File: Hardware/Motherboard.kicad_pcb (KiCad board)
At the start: 2 copper layers, 132.1 x 81.3 mm, 51 parts, among them J1 BME680, J2 Conn_01x05_Male, J3 Display_1, J4 Display_2, J5 Buttons, J6 USB, Q1 DMG3414U, SW1 Button_Plus, SW2 Button_Minus, SW3 Button_Settings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

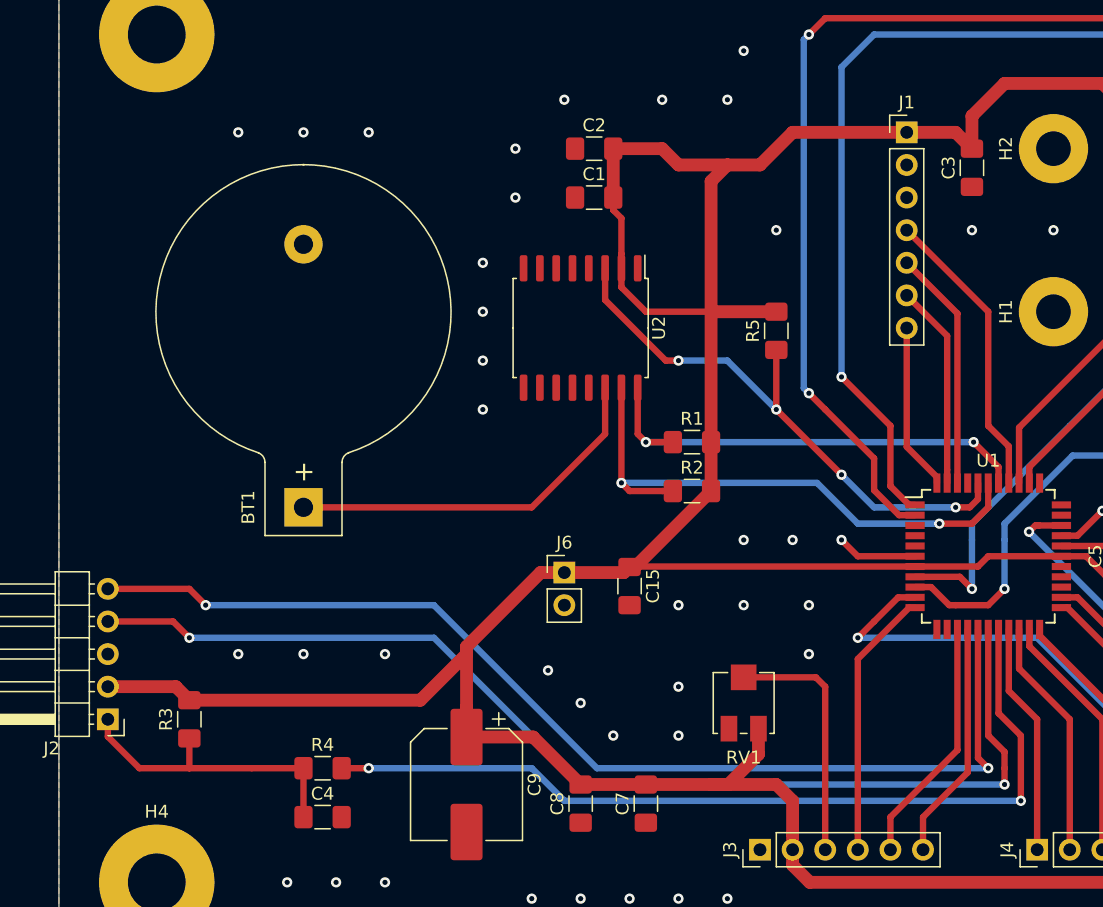
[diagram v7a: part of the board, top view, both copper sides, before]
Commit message: [Hardware] Swapped programming connector to have it in the right order.
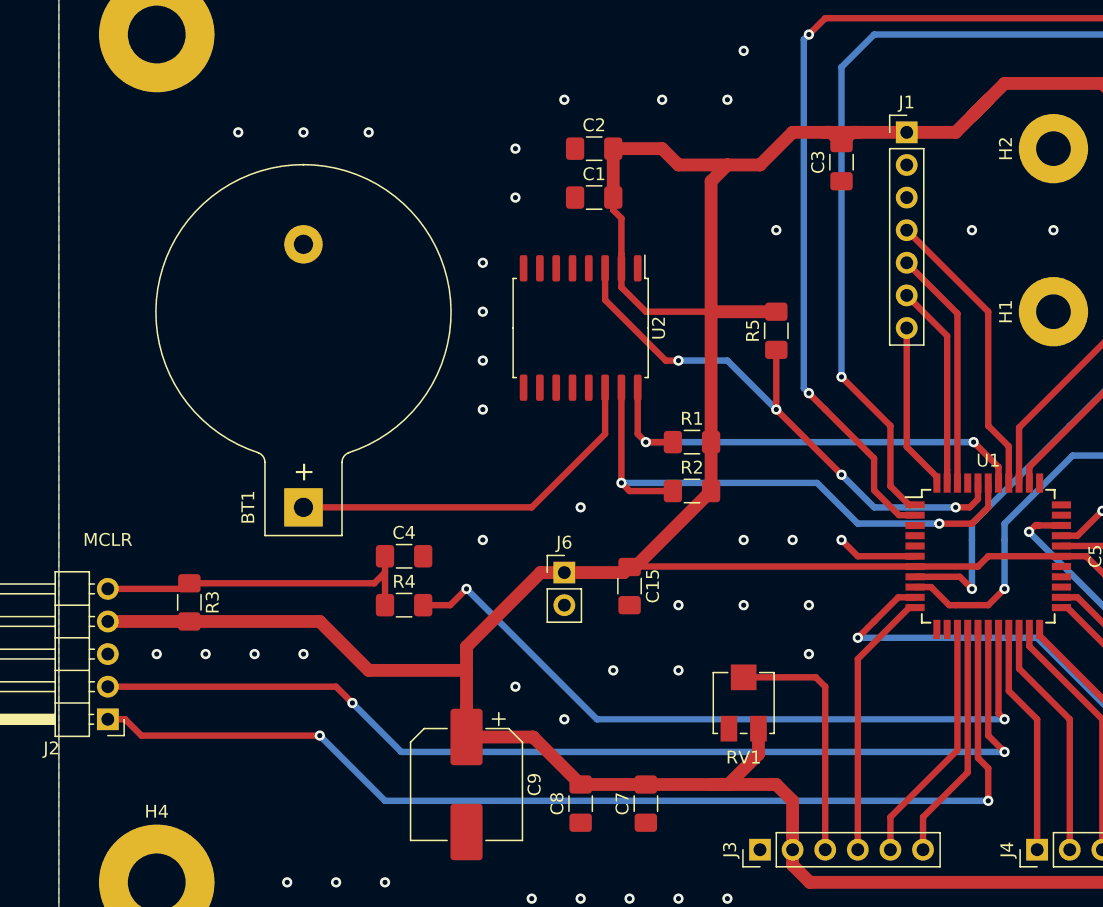
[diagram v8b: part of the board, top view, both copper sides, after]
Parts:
- J2: value Conn_01x05_Male -> JTAG
- moved C4 21.3 mm to (147.5, 55.9)
- moved R4 14.2 mm to (147.5, 59.7)
- moved C3 10.2 mm to (181.6, 25.2)
- moved R3 9.11 mm to (130.8, 59.5), turned to 270 degrees
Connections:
- H3 pad 1: Net-(H3-Pad1) -> GND
- H4 pad 1: Net-(H4-Pad1) -> GND
- H5 pad 1: Net-(H5-Pad1) -> GND
- H6 pad 1: Net-(H6-Pad1) -> GND
- J2 pad 1: Net-(C4-Pad1) -> Net-(J2-Pad1)
- J2 pad 2: +5V -> Net-(J2-Pad2)
- J2 pad 4: Net-(J2-Pad4) -> +5V
- J2 pad 5: Net-(J2-Pad5) -> Net-(C4-Pad1)
- U1 pad 16: Net-(J2-Pad5) -> Net-(J2-Pad1)
- U1 pad 17: Net-(J2-Pad4) -> Net-(J2-Pad2)
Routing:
- net Net-(J2-Pad4): track 87.7 -> 0.00 mm, vias 2 -> 0
- net Net-(J2-Pad5): track 85.5 -> 0.00 mm, vias 2 -> 0
- net Net-(J2-Pad1): track 0.00 -> 84.9 mm, vias 0 -> 2
- net Net-(J2-Pad2): track 0.00 -> 82.0 mm, vias 0 -> 2
- net /RE3: track 68.0 -> 57.2 mm
- net Net-(C4-Pad1): track 23.7 -> 25.9 mm
- net +5V: track 411.3 -> 413.4 mm
- net GND: vias 75 -> 77
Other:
- board text added: "MCLR"
